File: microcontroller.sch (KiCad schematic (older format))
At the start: 15 parts, among them U1 ATMEGA32U4

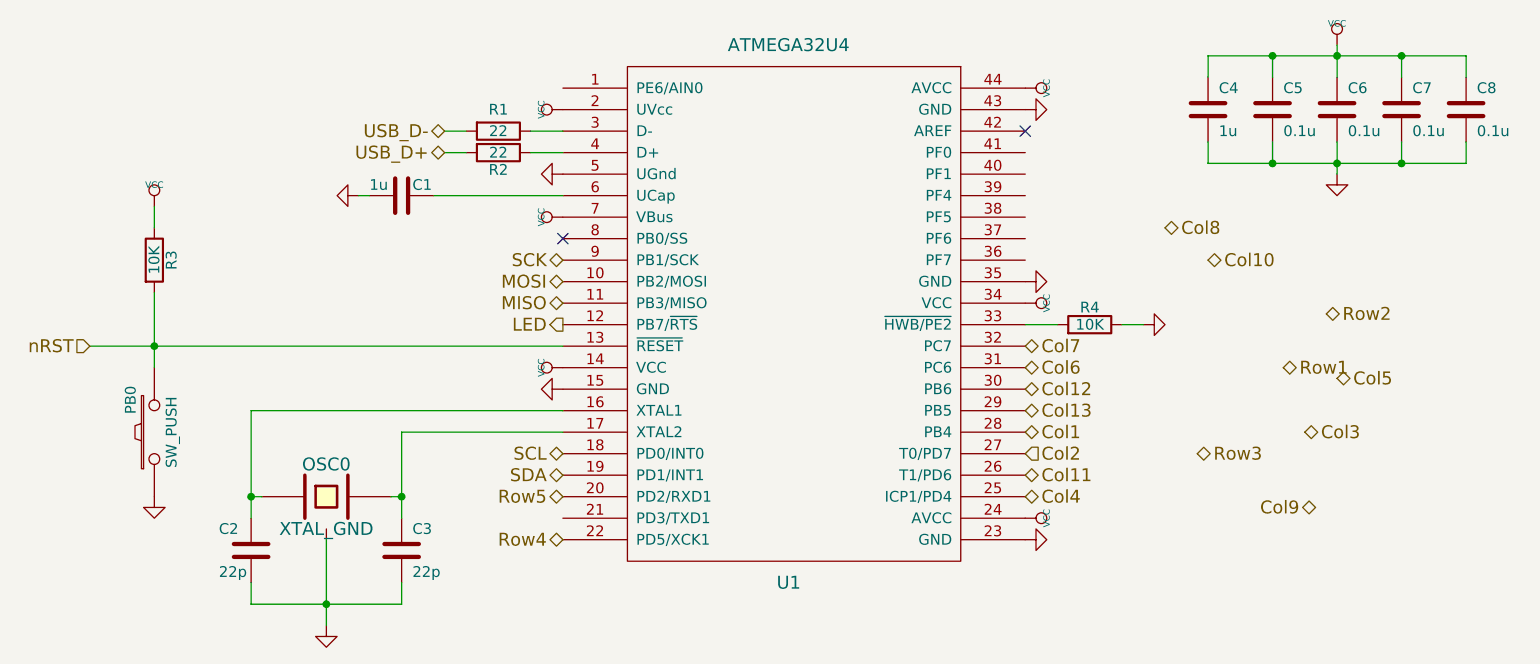
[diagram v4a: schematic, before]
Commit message: Focusing efforts on one main layout (semi-ortho), so that PCB-mounted and Alps components can be supported
Updated keenkeeb-reb1.png with new layout.
Started removing footprints and adding new spacebar footprints.
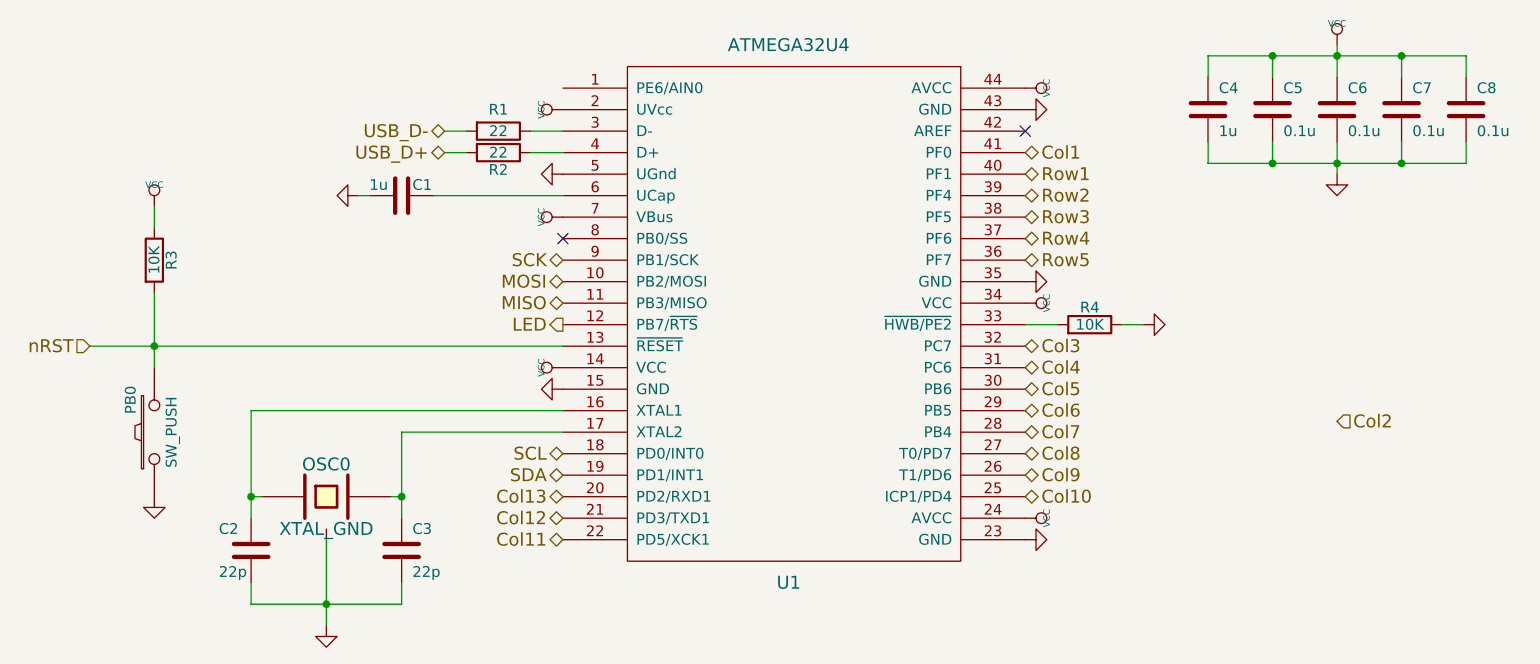
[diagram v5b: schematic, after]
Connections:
- net Col1: now also U1.41 (PF0); no longer U1.28 (PB4)
- net Col10: now also U1.25 (ICP1/PD4)
- net Col11: now also U1.22 (PD5/XCK1); no longer U1.26 (T1/PD6)
- net Col12: now also U1.21 (PD3/TXD1); no longer U1.30 (PB6)
- net Col13: now also U1.20 (PD2/RXD1); no longer U1.29 (PB5)
- net Col2: no longer U1.27 (T0/PD7)
- net Col3: now also U1.32 (PC7)
- net Col4: now also U1.31 (PC6); no longer U1.25 (ICP1/PD4)
- net Col5: now also U1.30 (PB6)
- net Col6: now also U1.29 (PB5); no longer U1.31 (PC6)
- net Col7: now also U1.28 (PB4); no longer U1.32 (PC7)
- net Col8: now also U1.27 (T0/PD7)
- net Col9: now also U1.26 (T1/PD6)
- net Row1: now also U1.40 (PF1)
- net Row2: now also U1.39 (PF4)
- net Row3: now also U1.38 (PF5)
- net Row4: now also U1.37 (PF6); no longer U1.22 (PD5/XCK1)
- net Row5: now also U1.36 (PF7); no longer U1.20 (PD2/RXD1)
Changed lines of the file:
@@
 	0    1    -1   0
 $EndComp
-Text HLabel 7100 5150 2    60   BiDi ~ 0
+Text HLabel 7100 4550 2    60   BiDi ~ 0
 Col4
-Text HLabel 7100 4550 2    60   BiDi ~ 0
+Text HLabel 7100 4750 2    60   BiDi ~ 0
 Col6
-Text HLabel 7750 3900 2    60   BiDi ~ 0
+Text HLabel 7100 4950 2    60   BiDi ~ 0
 Col8
+Text HLabel 4950 5250 0    60   BiDi ~ 0
+Col12
+Text HLabel 4950 5150 0    60   BiDi ~ 0
+Col13
+Text HLabel 4950 5350 0    60   BiDi ~ 0
+Col11
+Text HLabel 7100 5050 2    60   BiDi ~ 0
+Col9
+Text HLabel 7100 4850 2    60   BiDi ~ 0
+Col7
 Text HLabel 7100 4650 2    60   BiDi ~ 0
-Col12
-Text HLabel 7100 4750 2    60   BiDi ~ 0
-Col13
-Text HLabel 7100 5050 2    60   BiDi ~ 0
-Col11
-Text HLabel 8450 5200 0    60   BiDi ~ 0
-Col9
+Col5
 Text HLabel 7100 4450 2    60   BiDi ~ 0
-Col7
-Text HLabel 8550 4600 2    60   BiDi ~ 0
-Col5
-Text HLabel 8400 4850 2    60   BiDi ~ 0
 Col3
 $Comp
@@
 	8250 3500 8250 3600
 Connection ~ 8250 3600
-Text HLabel 7950 4050 2    60   BiDi ~ 0
+Text HLabel 7100 5150 2    60   BiDi ~ 0
 Col10
-Text HLabel 7900 4950 2    60   BiDi ~ 0
+Text HLabel 7100 3850 2    60   BiDi ~ 0
 Row3
-Text HLabel 4950 5350 0    60   BiDi ~ 0
+Text HLabel 7100 3950 2    60   BiDi ~ 0
 Row4
-Text HLabel 4950 5150 0    60   BiDi ~ 0
+Text HLabel 7100 4050 2    60   BiDi ~ 0
 Row5
-Text HLabel 7100 4950 2    60   Input ~ 0
+Text HLabel 8550 4800 2    60   Input ~ 0
 Col2
-Text HLabel 7100 4850 2    60   BiDi ~ 0
+Text HLabel 7100 3550 2    60   BiDi ~ 0
 Col1
-Text HLabel 8500 4300 2    60   BiDi ~ 0
+Text HLabel 7100 3750 2    60   BiDi ~ 0
 Row2
-Text HLabel 8300 4550 2    60   BiDi ~ 0
+Text HLabel 7100 3650 2    60   BiDi ~ 0
 Row1
 Text HLabel 4950 4950 0    60   BiDi ~ 0

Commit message: Started to layout with MX/Alps footprints
Added footprints that support Cherry MX and Alps switches.
Started to layout the board with new footprints.  Will support PCB
mounted switches/stabs.
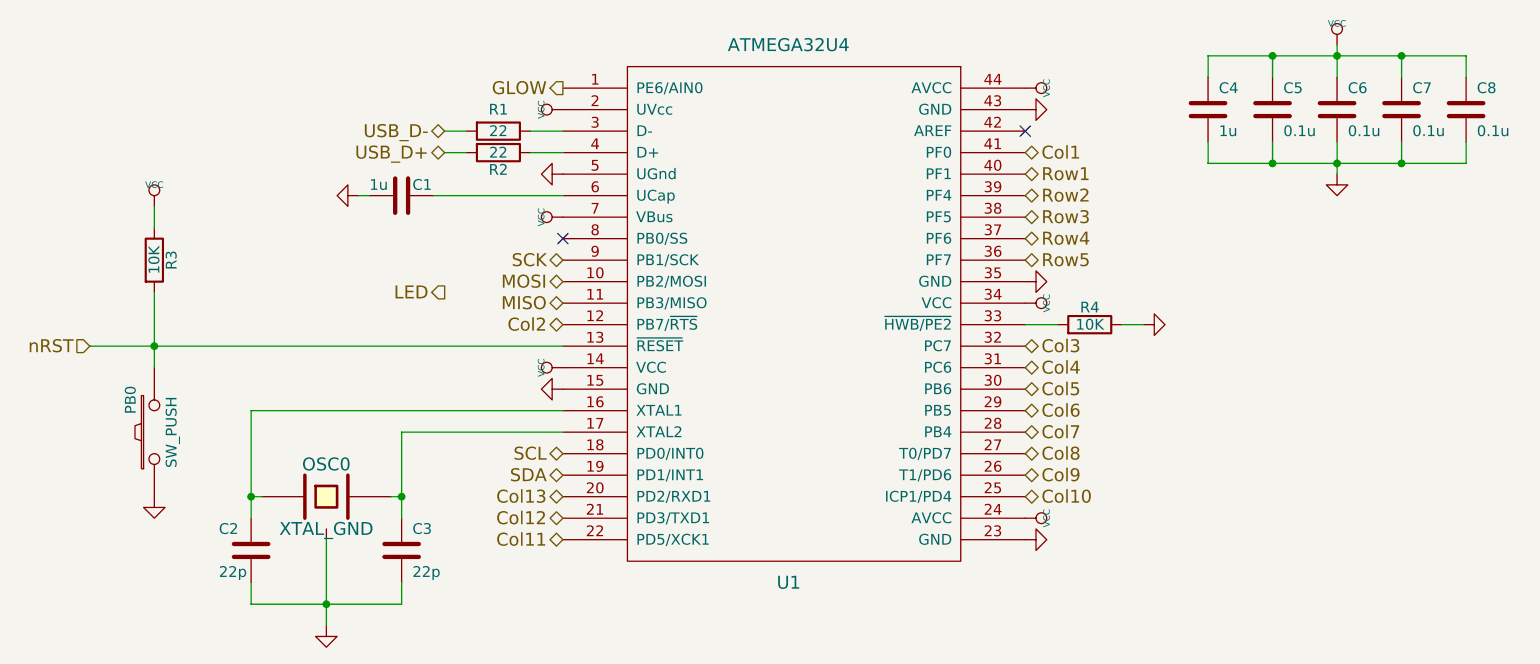
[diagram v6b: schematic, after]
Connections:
- net Col2: now also U1.12 (PB7/~RTS)
- net LED: no longer U1.12 (PB7/~RTS)
- net GLOW: now reaches U1.1 (PE6/AIN0)
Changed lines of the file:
@@
 Text HLabel 7100 4050 2    60   BiDi ~ 0
 Row5
-Text HLabel 8550 4800 2    60   Input ~ 0
+Text HLabel 4950 4350 0    60   BiDi ~ 0
 Col2
 Text HLabel 7100 3550 2    60   BiDi ~ 0
@@
 nRST
 NoConn ~ 4950 3950
-Text HLabel 4950 4350 0    60   Output ~ 0
+Text HLabel 4400 4200 0    60   Output ~ 0
 LED
 Wire Wire Line
@@
 Wire Wire Line
 	4400 3450 4500 3450
+Text HLabel 4950 3250 0    60   Output ~ 0
+GLOW
 $EndSCHEMATC

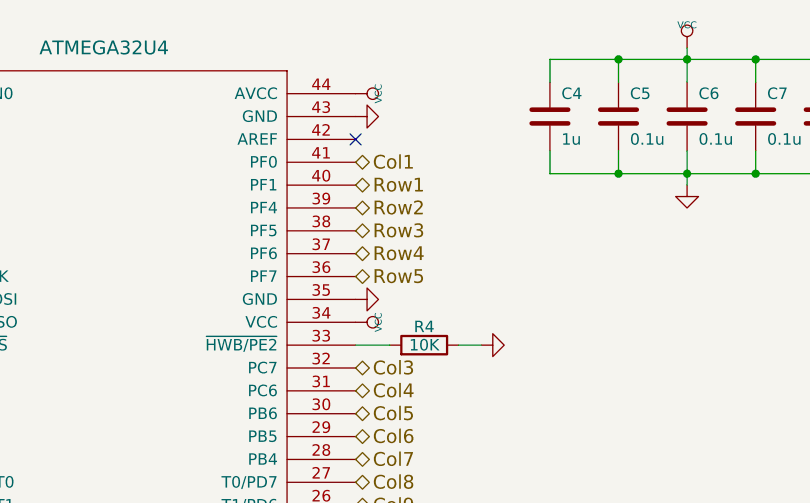
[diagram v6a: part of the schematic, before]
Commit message: Connected most of the components on the board
TODO:
Replace P1 with 1x6 header for SPI, Vcc, GND
Add test pads
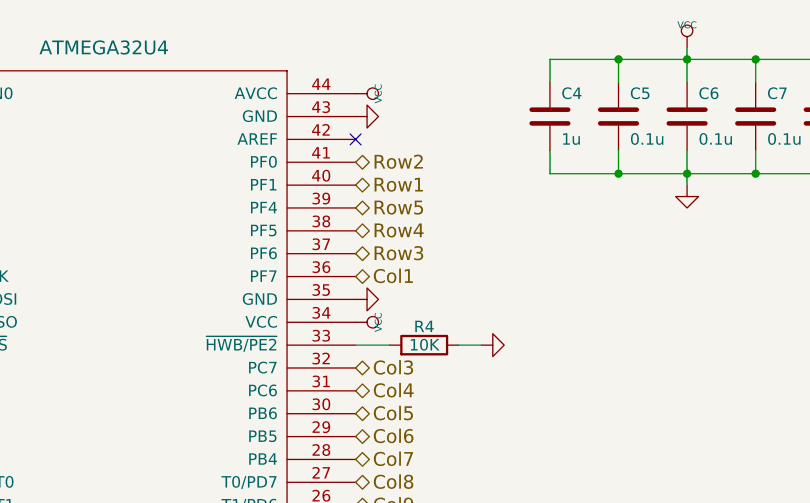
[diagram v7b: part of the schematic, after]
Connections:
- net Col1: now also U1.36 (PF7); no longer U1.41 (PF0)
- net Row2: now also U1.41 (PF0); no longer U1.39 (PF4)
- net Row3: now also U1.37 (PF6); no longer U1.38 (PF5)
- net Row4: now also U1.38 (PF5); no longer U1.37 (PF6)
- net Row5: now also U1.39 (PF4); no longer U1.36 (PF7)
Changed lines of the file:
@@
 P 4000 3750
 AR Path="/587C033B" Ref="#PWR08"  Part="1"
-AR Path="/585C991A/587C033B" Ref="#PWR08"  Part="1"
-F 0 "#PWR08" H 4000 3750 30  0001 C CNN
+AR Path="/585C991A/587C033B" Ref="#PWR010"  Part="1"
+F 0 "#PWR010" H 4000 3750 30  0001 C CNN
 F 1 "GND" H 4000 3680 30  0001 C CNN
 F 2 "" H 4000 3750 60  0001 C CNN
@@
 P 4950 3650
 AR Path="/587C0359" Ref="#PWR09"  Part="1"
-AR Path="/585C991A/587C0359" Ref="#PWR09"  Part="1"
-F 0 "#PWR09" H 4950 3650 30  0001 C CNN
+AR Path="/585C991A/587C0359" Ref="#PWR011"  Part="1"
+F 0 "#PWR011" H 4950 3650 30  0001 C CNN
 F 1 "GND" H 4950 3580 30  0001 C CNN
 F 2 "" H 4950 3650 60  0001 C CNN
@@
 	4350 3750 4950 3750
 $Comp
-L VCC #PWR010
+L VCC #PWR012
 U 1 1 587C0686
 P 4950 3850
-F 0 "#PWR010" H 4950 3950 30  0001 C CNN
+F 0 "#PWR012" H 4950 3950 30  0001 C CNN
 F 1 "VCC" H 4950 3950 30  0000 C CNN
 F 2 "" H 4950 3850 60  0001 C CNN
@@
 $EndComp
 $Comp
-L VCC #PWR011
+L VCC #PWR013
 U 1 1 587C07FD
 P 4950 3350
-F 0 "#PWR011" H 4950 3450 30  0001 C CNN
+F 0 "#PWR013" H 4950 3450 30  0001 C CNN
 F 1 "VCC" H 4950 3450 30  0000 C CNN
 F 2 "" H 4950 3350 60  0001 C CNN
@@
 $EndComp
 $Comp
-L VCC #PWR012
+L VCC #PWR014
 U 1 1 587C0959
 P 7100 3250
-F 0 "#PWR012" H 7100 3350 30  0001 C CNN
+F 0 "#PWR014" H 7100 3350 30  0001 C CNN
 F 1 "VCC" H 7100 3350 30  0000 C CNN
 F 2 "" H 7100 3250 60  0001 C CNN
@@
 $EndComp
 $Comp
-L VCC #PWR013
+L VCC #PWR015
 U 1 1 587C0977
 P 7100 4250
-F 0 "#PWR013" H 7100 4350 30  0001 C CNN
+F 0 "#PWR015" H 7100 4350 30  0001 C CNN
 F 1 "VCC" H 7100 4350 30  0000 C CNN
 F 2 "" H 7100 4250 60  0001 C CNN
@@
 $EndComp
 $Comp
-L VCC #PWR014
+L VCC #PWR016
 U 1 1 587C0995
 P 7100 5250
-F 0 "#PWR014" H 7100 5350 30  0001 C CNN
+F 0 "#PWR016" H 7100 5350 30  0001 C CNN
 F 1 "VCC" H 7100 5350 30  0000 C CNN
 F 2 "" H 7100 5250 60  0001 C CNN
@@
 P 7100 5350
 AR Path="/587C0B0C" Ref="#PWR015"  Part="1"
-AR Path="/585C991A/587C0B0C" Ref="#PWR015"  Part="1"
-F 0 "#PWR015" H 7100 5350 30  0001 C CNN
+AR Path="/585C991A/587C0B0C" Ref="#PWR017"  Part="1"
+F 0 "#PWR017" H 7100 5350 30  0001 C CNN
 F 1 "GND" H 7100 5280 30  0001 C CNN
 F 2 "" H 7100 5350 60  0001 C CNN
@@
 P 7100 4150
 AR Path="/587C0B2A" Ref="#PWR016"  Part="1"
-AR Path="/585C991A/587C0B2A" Ref="#PWR016"  Part="1"
-F 0 "#PWR016" H 7100 4150 30  0001 C CNN
+AR Path="/585C991A/587C0B2A" Ref="#PWR018"  Part="1"
+F 0 "#PWR018" H 7100 4150 30  0001 C CNN
 F 1 "GND" H 7100 4080 30  0001 C CNN
 F 2 "" H 7100 4150 60  0001 C CNN
@@
 P 4950 4650
 AR Path="/587C0B5C" Ref="#PWR017"  Part="1"
-AR Path="/585C991A/587C0B5C" Ref="#PWR017"  Part="1"
-F 0 "#PWR017" H 4950 4650 30  0001 C CNN
+AR Path="/585C991A/587C0B5C" Ref="#PWR019"  Part="1"
+F 0 "#PWR019" H 4950 4650 30  0001 C CNN
 F 1 "GND" H 4950 4580 30  0001 C CNN
 F 2 "" H 4950 4650 60  0001 C CNN
@@
 $EndComp
 $Comp
-L VCC #PWR018
+L VCC #PWR020
 U 1 1 587C0BAE
 P 4950 4550
-F 0 "#PWR018" H 4950 4650 30  0001 C CNN
+F 0 "#PWR020" H 4950 4650 30  0001 C CNN
 F 1 "VCC" H 4950 4650 30  0000 C CNN
 F 2 "" H 4950 4550 60  0001 C CNN
@@
 $EndComp
 $Comp
-L VCC #PWR019
+L VCC #PWR021
 U 1 1 587C0CDD
 P 3050 3800
-F 0 "#PWR019" H 3050 3900 30  0001 C CNN
+F 0 "#PWR021" H 3050 3900 30  0001 C CNN
 F 1 "VCC" H 3050 3900 30  0000 C CNN
 F 2 "" H 3050 3800 60  0001 C CNN
@@
 P 3050 5150
 AR Path="/587C0E1E" Ref="#PWR020"  Part="1"
-AR Path="/585C991A/587C0E1E" Ref="#PWR020"  Part="1"
-F 0 "#PWR020" H 3050 5150 30  0001 C CNN
+AR Path="/585C991A/587C0E1E" Ref="#PWR022"  Part="1"
+F 0 "#PWR022" H 3050 5150 30  0001 C CNN
 F 1 "GND" H 3050 5080 30  0001 C CNN
 F 2 "" H 3050 5150 60  0001 C CNN
@@
 P 3850 5750
 AR Path="/587C1B56" Ref="#PWR021"  Part="1"
-AR Path="/585C991A/587C1B56" Ref="#PWR021"  Part="1"
-F 0 "#PWR021" H 3850 5750 30  0001 C CNN
+AR Path="/585C991A/587C1B56" Ref="#PWR023"  Part="1"
+F 0 "#PWR023" H 3850 5750 30  0001 C CNN
 F 1 "GND" H 3850 5680 30  0001 C CNN
 F 2 "" H 3850 5750 60  0001 C CNN
@@
 P 7100 3350
 AR Path="/587C2147" Ref="#PWR022"  Part="1"
-AR Path="/585C991A/587C2147" Ref="#PWR022"  Part="1"
-F 0 "#PWR022" H 7100 3350 30  0001 C CNN
+AR Path="/585C991A/587C2147" Ref="#PWR024"  Part="1"
+F 0 "#PWR024" H 7100 3350 30  0001 C CNN
 F 1 "GND" H 7100 3280 30  0001 C CNN
 F 2 "" H 7100 3350 60  0001 C CNN
@@
 P 7650 4350
 AR Path="/587C2382" Ref="#PWR023"  Part="1"
-AR Path="/585C991A/587C2382" Ref="#PWR023"  Part="1"
-F 0 "#PWR023" H 7650 4350 30  0001 C CNN
+AR Path="/585C991A/587C2382" Ref="#PWR025"  Part="1"
+F 0 "#PWR025" H 7650 4350 30  0001 C CNN
 F 1 "GND" H 7650 4280 30  0001 C CNN
 F 2 "" H 7650 4350 60  0001 C CNN
@@
 Connection ~ 3050 4450
 $Comp
-L VCC #PWR024
+L VCC #PWR026
 U 1 1 587C8EA3
 P 8550 3050
-F 0 "#PWR024" H 8550 3150 30  0001 C CNN
+F 0 "#PWR026" H 8550 3150 30  0001 C CNN
 F 1 "VCC" H 8550 3150 30  0000 C CNN
 F 2 "" H 8550 3050 60  0001 C CNN
@@
 P 8550 3650
 AR Path="/587C8ECB" Ref="#PWR025"  Part="1"
-AR Path="/585C991A/587C8ECB" Ref="#PWR025"  Part="1"
-F 0 "#PWR025" H 8550 3650 30  0001 C CNN
+AR Path="/585C991A/587C8ECB" Ref="#PWR027"  Part="1"
+F 0 "#PWR027" H 8550 3650 30  0001 C CNN
 F 1 "GND" H 8550 3580 30  0001 C CNN
 F 2 "" H 8550 3650 60  0001 C CNN
@@
 Text HLabel 7100 5150 2    60   BiDi ~ 0
 Col10
+Text HLabel 7100 3950 2    60   BiDi ~ 0
+Row3
 Text HLabel 7100 3850 2    60   BiDi ~ 0
-Row3
-Text HLabel 7100 3950 2    60   BiDi ~ 0
 Row4
-Text HLabel 7100 4050 2    60   BiDi ~ 0
+Text HLabel 7100 3750 2    60   BiDi ~ 0
 Row5
 Text HLabel 4950 4350 0    60   BiDi ~ 0
 Col2
+Text HLabel 7100 4050 2    60   BiDi ~ 0
+Col1
 Text HLabel 7100 3550 2    60   BiDi ~ 0
-Col1
-Text HLabel 7100 3750 2    60   BiDi ~ 0
 Row2
 Text HLabel 7100 3650 2    60   BiDi ~ 0

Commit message: More progress on PCB
Cleaned up silkscreen layers
Updated switch footprints to remove front layer and hide reference on
back layer
Moved references on back layer
Moved bottom mounting holes on PCB
Cleaned up matrix schematic
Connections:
- net SS: now reaches U1.8 (PB0/SS)
- no-connect marks 2 -> 1
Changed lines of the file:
@@
 Text HLabel 2750 4450 0    60   Input ~ 0
 nRST
-NoConn ~ 4950 3950
-Text HLabel 4400 4200 0    60   Output ~ 0
-LED
 Wire Wire Line
 	3050 3900 3050 3800
@@
 Text HLabel 4950 3250 0    60   Output ~ 0
 GLOW
+Text HLabel 4950 3950 0    60   BiDi ~ 0
+SS
 $EndSCHEMATC
